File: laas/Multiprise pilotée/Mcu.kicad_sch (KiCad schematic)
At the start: 0 parts

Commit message: Sauvegarde du travail en cours
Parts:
- added U8: MOUDLE-SEEEDUINO-XIAO, XIAO_PCB:MOUDLE14P-SMD-2.54-21X17.8MM, symbol MOUDLE-SEEEDUINO-XIAO:MOUDLE-SEEEDUINO-XIAO
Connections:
- new net +3V3: U8.12 (3V3)
- new net CS_PWR_DC: U8.2 (PA4_A1_D1)
- new net GND: U8.13 (GND)
- new net LATCH: U8.3 (PA10_A2_D2)
- new net PWM_VAR_PWR: U8.5 (PA8_A4_D4_SDA)
- new net SPI_MOSI: U8.11 (PA6_A10_D10_MOSI)
- new net SPI_SCK: U8.9 (PA7_A8_D8_SCK)
- new net ~{CS_RELAY}: U8.1 (PA02_A0_D0)
- new net ~{RESET_IO}: U8.4 (PA11_A3_D3)
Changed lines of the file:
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@@
 (kicad_sch (version 20230121) (generator eeschema)
   (paper "A4")
+  (wire (pts (xy 104.14 53.34) (xy 124.46 53.34))
+    (stroke (width 0) (type default))
+  )
+  (wire (pts (xy 104.14 48.26) (xy 124.46 48.26))
+    (stroke (width 0) (type default))
+  )
+  (wire (pts (xy 44.45 43.18) (xy 63.5 43.18))
+    (stroke (width 0) (type default))
+  )
+  (wire (pts (xy 44.45 45.72) (xy 63.5 45.72))
+    (stroke (width 0) (type default))
+  )
+  (wire (pts (xy 63.5 50.8) (xy 44.45 50.8))
+    (stroke (width 0) (type default))
+  )
+  (wire (pts (xy 104.14 43.18) (xy 107.95 43.18))
+    (stroke (width 0) (type default))
+  )
+  (wire (pts (xy 104.14 45.72) (xy 111.76 45.72))
+    (stroke (width 0) (type default))
+  )
+  (wire (pts (xy 111.76 36.83) (xy 111.76 45.72))
+    (stroke (width 0) (type default))
+  )
+  (wire (pts (xy 44.45 48.26) (xy 63.5 48.26))
+    (stroke (width 0) (type default))
+  )
+  (wire (pts (xy 44.45 40.64) (xy 63.5 40.64))
+    (stroke (width 0) (type default))
+  )
+  (wire (pts (xy 107.95 43.18) (xy 107.95 59.69))
+    (stroke (width 0) (type default))
+  )
+  (hierarchical_label "LATCH" (shape input) (at 44.45 45.72 180) (fields_autoplaced)
+    (effects (font (size 1.27 1.27)) (justify right))
+  )
+  (hierarchical_label "~{RESET_IO}" (shape input) (at 44.45 48.26 180) (fields_autoplaced)
+    (effects (font (size 1.27 1.27)) (justify right))
+  )
+  (hierarchical_label "CS_PWR_DC" (shape input) (at 44.45 43.18 180) (fields_autoplaced)
+    (effects (font (size 1.27 1.27)) (justify right))
+  )
+  (hierarchical_label "PWM_VAR_PWR" (shape input) (at 44.45 50.8 180) (fields_autoplaced)
+    (effects (font (size 1.27 1.27)) (justify right))
+  )
+  (hierarchical_label "~{CS_RELAY}" (shape input) (at 44.45 40.64 180) (fields_autoplaced)
+    (effects (font (size 1.27 1.27)) (justify right))
+  )
+  (hierarchical_label "SPI_SCK" (shape input) (at 124.46 53.34 0) (fields_autoplaced)
+    (effects (font (size 1.27 1.27)) (justify left))
+  )
+  (hierarchical_label "SPI_MOSI" (shape input) (at 124.46 48.26 0) (fields_autoplaced)
+    (effects (font (size 1.27 1.27)) (justify left))
+  )
+  (symbol (lib_id "power:+3V3") (at 111.76 36.83 0) (unit 1)
+    (in_bom yes) (on_board yes) (dnp no) (fields_autoplaced)
+    (property "Reference" "#PWR036" (at 111.76 40.64 0)
+      (effects (font (size 1.27 1.27)) hide)
+    )
+    (property "Value" "+3V3" (at 111.76 31.75 0)
+      (effects (font (size 1.27 1.27)))
+    )
+    (property "Footprint" "" (at 111.76 36.83 0)
+      (effects (font (size 1.27 1.27)) hide)
+    )
+    (property "Datasheet" "" (at 111.76 36.83 0)
+      (effects (font (size 1.27 1.27)) hide)
+    )
+    (pin "1")
+    (instances
+      (project "Multiprise pilotée"
+        (path "/ad17dd83-c10a-426e-803d-3b2dda0cc379/5b1c34c0-fac2-48fe-a40d-d33e3b5a6f25"
+          (reference "#PWR036") (unit 1)
+        )
+      )
+    )
+  )
+  (symbol (lib_id "power:GND") (at 107.95 59.69 0) (unit 1)
+    (in_bom yes) (on_board yes) (dnp no) (fields_autoplaced)
+    (property "Reference" "#PWR037" (at 107.95 66.04 0)
+      (effects (font (size 1.27 1.27)) hide)
+    )
+    (property "Value" "GND" (at 107.95 64.77 0)
+      (effects (font (size 1.27 1.27)))
+    )
+    (property "Footprint" "" (at 107.95 59.69 0)
+      (effects (font (size 1.27 1.27)) hide)
+    )
+    (property "Datasheet" "" (at 107.95 59.69 0)
+      (effects (font (size 1.27 1.27)) hide)
+    )
+    (pin "1")
+    (instances
+      (project "Multiprise pilotée"
+        (path "/ad17dd83-c10a-426e-803d-3b2dda0cc379/5b1c34c0-fac2-48fe-a40d-d33e3b5a6f25"
+          (reference "#PWR037") (unit 1)
+        )
+      )
+    )
+  )
+  (symbol (lib_id "MOUDLE-SEEEDUINO-XIAO:MOUDLE-SEEEDUINO-XIAO") (at 82.55 48.26 0) (unit 1)
+    (in_bom yes) (on_board yes) (dnp no) (fields_autoplaced)
+    (property "Reference" "U8" (at 83.82 33.02 0)
+      (effects (font (size 1.27 1.27)))
+    )
+    (property "Value" "MOUDLE-SEEEDUINO-XIAO" (at 83.82 35.56 0)
+      (effects (font (size 1.27 1.27)))
+    )
+    (property "Footprint" "XIAO_PCB:MOUDLE14P-SMD-2.54-21X17.8MM" (at 66.04 45.72 0)
+      (effects (font (size 1.27 1.27)) hide)
+    )
+    (property "Datasheet" "" (at 66.04 45.72 0)
+      (effects (font (size 1.27 1.27)) hide)
+    )
+    (pin "7")
+    (pin "9")
+    (pin "8")
+    (pin "13")
+    (pin "5")
+    (pin "4")
+    (pin "14")
+    (pin "11")
+    (pin "1")
+    (pin "2")
+    (pin "6")
+    (pin "12")
+    (pin "10")
+    (pin "3")
+    (instances
+      (project "Multiprise pilotée"
+        (path "/ad17dd83-c10a-426e-803d-3b2dda0cc379/5b1c34c0-fac2-48fe-a40d-d33e3b5a6f25"
+          (reference "U8") (unit 1)
+        )
+      )
+    )
+  )
 )

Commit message: Commit de propreté
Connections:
- no-connect marks 0 -> 5
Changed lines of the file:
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@@
 (kicad_sch (version 20230121) (generator eeschema)
   (paper "A4")
+  (no_connect (at 104.14 40.64))
+  (no_connect (at 104.14 55.88))
+  (no_connect (at 104.14 50.8))
+  (no_connect (at 63.5 55.88))
+  (no_connect (at 63.5 53.34))
   (wire (pts (xy 104.14 53.34) (xy 124.46 53.34))
     (stroke (width 0) (type default))

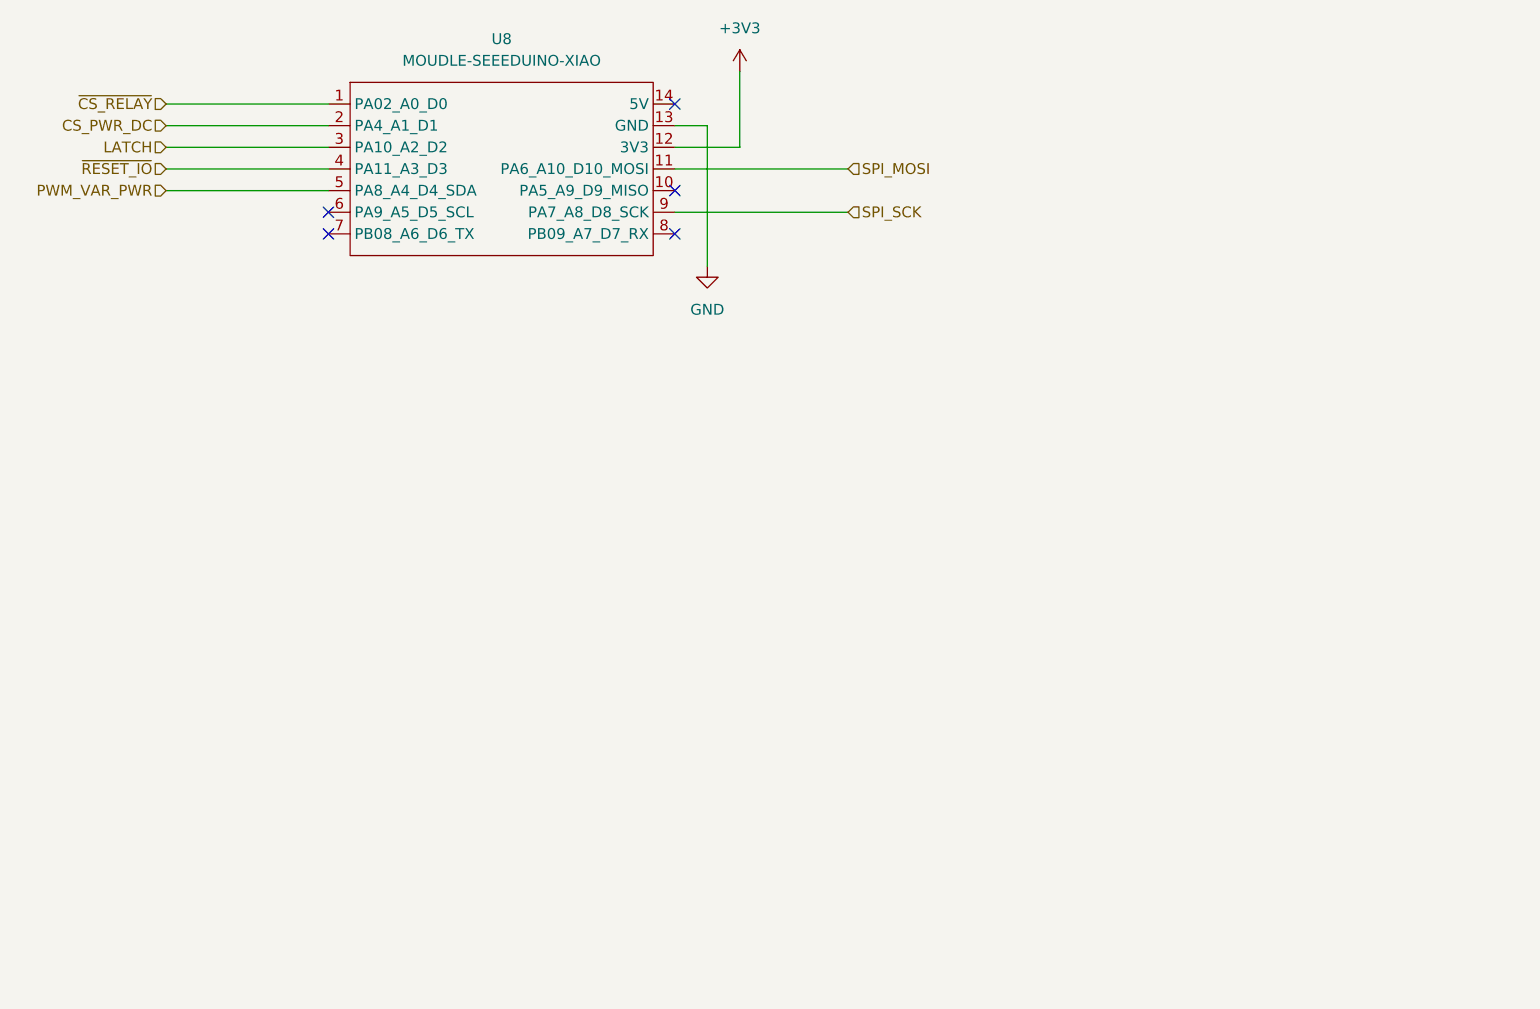
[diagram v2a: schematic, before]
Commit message: Nouvelle version PCB multiprise 1.3 avec suppresion des alim vpol et var
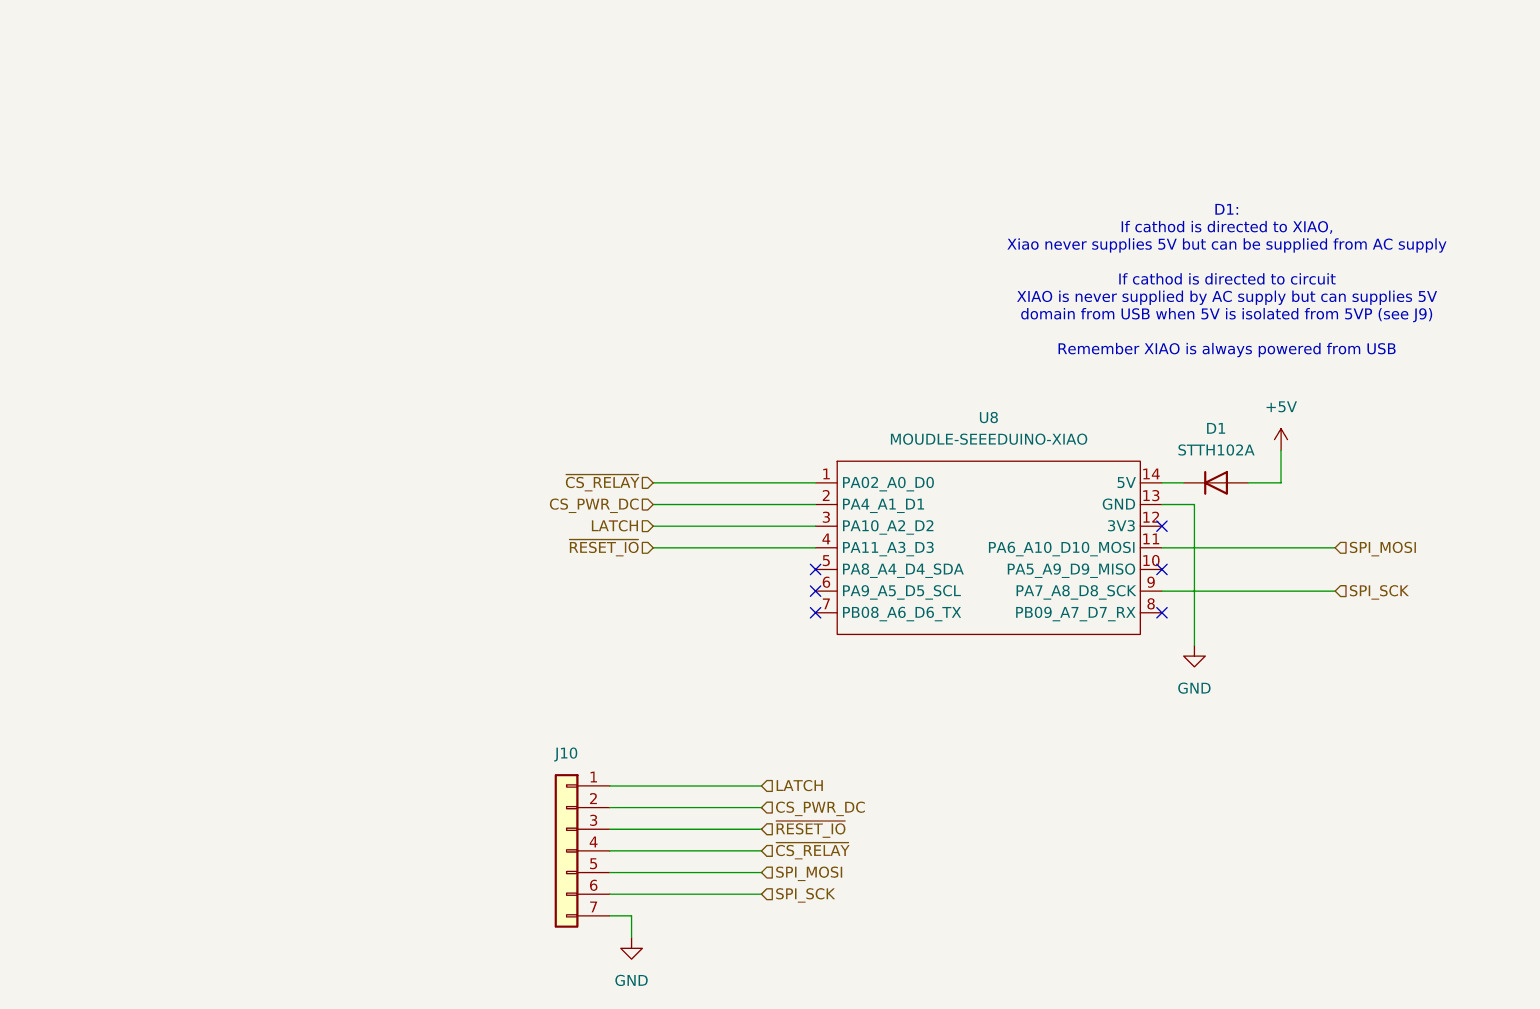
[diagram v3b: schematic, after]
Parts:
- added D1: STTH102A, Diode_SMD:D_SMA, symbol Device:D
- added J10: Conn_01x05, Connector_PinHeader_2.54mm:PinHeader_1x07_P2.54mm_Vertical, symbol Connector_Generic:Conn_01x07
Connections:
- net CS_PWR_DC: now also J10.2 (Pin_2)
- net GND: now also J10.7 (Pin_7)
- net LATCH: now also J10.1 (Pin_1)
- net SPI_MOSI: now also J10.5 (Pin_5)
- net SPI_SCK: now also J10.6 (Pin_6)
- net ~{CS_RELAY}: now also J10.4 (Pin_4)
- net ~{RESET_IO}: now also J10.3 (Pin_3)
- net at U8.14 (5V): now also D1.1 (K)
- net +3V3: no longer names the net of U8.12 (3V3)
- net PWM_VAR_PWR: no longer names the net of U8.5 (PA8_A4_D4_SDA)
- new net +5V: D1.2 (A)
- no-connect marks 5 -> 6
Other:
- note added: "D1: If cathod is directed to XIAO, Xiao never supplies 5V but can be supplied from AC supply If cathod is directed to circuit XIAO is never supplied by AC supply but can supplies 5V domain from USB when 5V is isolated from 5VP (see J9) Remember XIAO is always powered from USB"
- company: (none) -> INSA - GEI
- title: (none) -> Multiprise - MCU
- moved on the sheet: U8
